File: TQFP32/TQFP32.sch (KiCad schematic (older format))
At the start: 4 parts, among them J1 Conn_01x16, J2 Conn_01x16, J3 Conn_02x16_Counter_Clockwise, J4 Conn_02x16_Counter_Clockwise

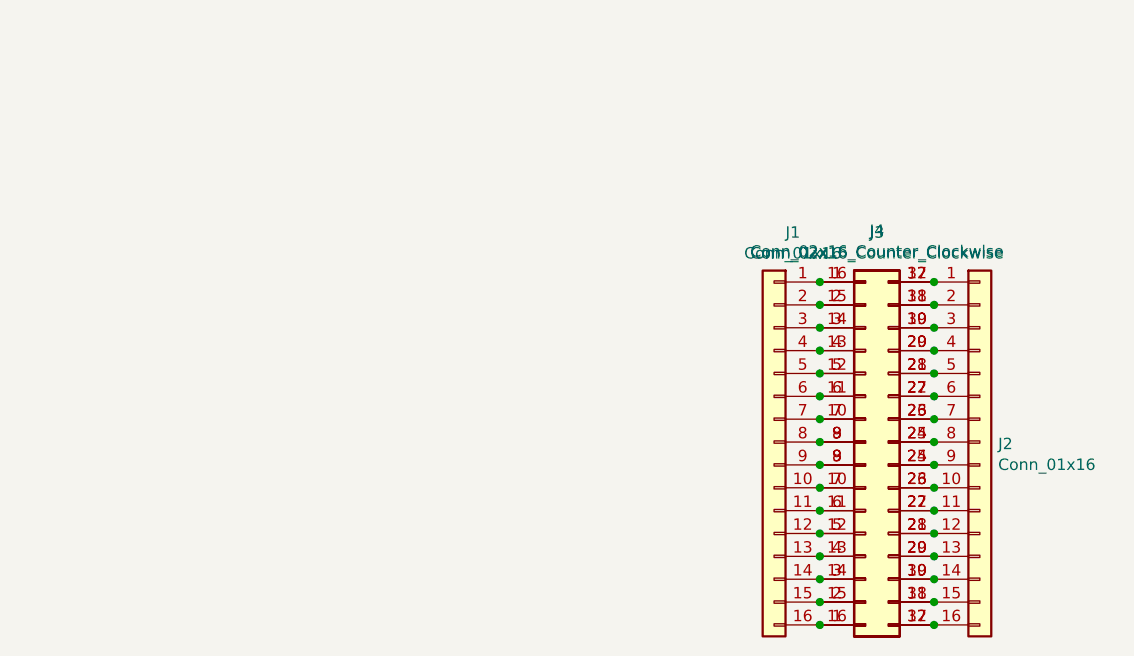
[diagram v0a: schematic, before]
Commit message: USB, SD and CR Cells Added
MicroSD, MicroUSB, MiniUSB, USB-C, CR1220, CR2032 added as well as all schematics page sizes optimised
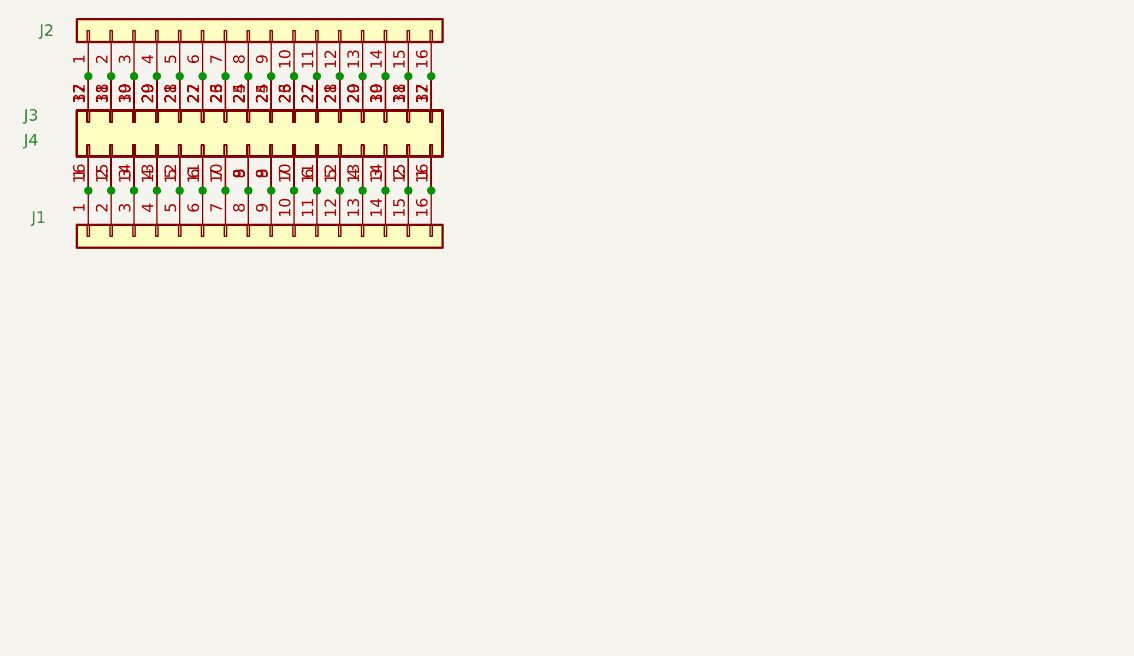
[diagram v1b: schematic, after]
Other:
- moved on the sheet: J1, J2, J3, J4
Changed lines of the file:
@@
 EESchema Schematic File Version 4
+LIBS:TQFP32-cache
 EELAYER 29 0
 EELAYER END
-$Descr A4 11693 8268
+$Descr User 5197 4016
 encoding utf-8
 Sheet 1 1
-Title ""
-Date ""
-Rev ""
-Comp ""
-Comment1 ""
-Comment2 ""
-Comment3 ""
+Title "TQFP32 to DIP32 Breakout Board"
+Date "2019-07-04"
+Rev "1"
+Comp "SirBoard"
+Comment1 "TQFP32 P = 0.8mm"
+Comment2 "LQFP32 P = 0.5mm"
+Comment3 "DIP32 P = 2.54mm"
 Comment4 ""
 $EndDescr
@@
 L Connector_Generic:Conn_01x16 J2
 U 1 1 5D1E2D5B
-P 5750 2700
-F 0 "J2" H 5830 2692 50  0000 L CNN
-F 1 "Conn_01x16" H 5830 2601 50  0000 L CNN
-F 2 "Connector_PinHeader_2.54mm:PinHeader_1x16_P2.54mm_Vertical" H 5750 2700 50  0001 C CNN
-F 3 "~" H 5750 2700 50  0001 C CNN
-	1    5750 2700
-	1    0    0    -1
+P 2550 900
+F 0 "J2" V 2550 1750 50  0000 L CNN
+F 1 "Conn_01x16" V 2630 801 50  0001 L CNN
+F 2 "Connector_PinHeader_2.54mm:PinHeader_1x16_P2.54mm_Vertical" H 2550 900 50  0001 C CNN
+F 3 "~" H 2550 900 50  0001 C CNN
+	1    2550 900
+	0    -1   -1   0
 $EndComp
 $Comp
 L Connector_Generic:Conn_02x16_Counter_Clockwise J3
 U 1 1 5D1E33BB
-P 5250 2700
-F 0 "J3" H 5300 3617 50  0000 C CNN
-F 1 "Conn_02x16_Counter_Clockwise" H 5300 3526 50  0000 C CNN
-F 2 "Package_QFP:TQFP-32_7x7mm_P0.8mm" H 5250 2700 50  0001 C CNN
-F 3 "~" H 5250 2700 50  0001 C CNN
-	1    5250 2700
-	1    0    0    -1
+P 2550 1400
+F 0 "J3" V 2650 2350 50  0000 C TNN
+F 1 "Conn_02x16_Counter_Clockwise" H 2600 2226 50  0001 C CNN
+F 2 "Package_QFP:TQFP-32_7x7mm_P0.8mm" H 2550 1400 50  0001 C CNN
+F 3 "~" H 2550 1400 50  0001 C CNN
+	1    2550 1400
+	0    -1   -1   0
 $EndComp
 $Comp
 L Connector_Generic:Conn_01x16 J1
 U 1 1 5D1E5C1F
-P 4850 2700
-F 0 "J1" H 4768 3617 50  0000 C CNN
-F 1 "Conn_01x16" H 4768 3526 50  0000 C CNN
-F 2 "Connector_PinHeader_2.54mm:PinHeader_1x16_P2.54mm_Vertical" H 4850 2700 50  0001 C CNN
-F 3 "~" H 4850 2700 50  0001 C CNN
-	1    4850 2700
-	-1   0    0    -1
+P 2550 1800
+F 0 "J1" V 2468 2717 50  0000 C CNN
+F 1 "Conn_01x16" H 2468 2626 50  0001 C CNN
+F 2 "Connector_PinHeader_2.54mm:PinHeader_1x16_P2.54mm_Vertical" H 2550 1800 50  0001 C CNN
+F 3 "~" H 2550 1800 50  0001 C CNN
+	1    2550 1800
+	0    -1   1    0
 $EndComp
 $Comp
 L Connector_Generic:Conn_02x16_Counter_Clockwise J4
 U 1 1 5D1ED9F2
-P 5250 2800
-F 0 "J4" H 5300 1775 50  0000 C CNN
-F 1 "Conn_02x16_Counter_Clockwise" H 5300 1866 50  0000 C CNN
-F 2 "Package_QFP:LQFP-32_5x5mm_P0.5mm" H 5250 2800 50  0001 C CNN
-F 3 "~" H 5250 2800 50  0001 C CNN
-	1    5250 2800
-	1    0    0    1
+P 2650 1400
+F 0 "J4" V 2700 350 50  0000 C BNN
+F 1 "Conn_02x16_Counter_Clockwise" H 2700 466 50  0001 C CNN
+F 2 "Package_QFP:LQFP-32_5x5mm_P0.5mm" H 2650 1400 50  0001 C CNN
+F 3 "~" H 2650 1400 50  0001 C CNN
+	1    2650 1400
+	0    1    -1   0
 $EndComp
-Connection ~ 5050 2000
-Connection ~ 5050 2100
-Connection ~ 5050 2200
-Connection ~ 5050 2300
-Connection ~ 5050 2400
-Connection ~ 5050 2500
-Connection ~ 5050 2600
-Connection ~ 5050 2700
-Connection ~ 5050 2800
-Connection ~ 5050 2900
-Connection ~ 5050 3000
-Connection ~ 5050 3100
-Connection ~ 5050 3200
-Connection ~ 5050 3300
-Connection ~ 5050 3400
-Connection ~ 5050 3500
-Connection ~ 5550 2000
-Connection ~ 5550 2100
-Connection ~ 5550 2200
-Connection ~ 5550 2300
-Connection ~ 5550 2400
-Connection ~ 5550 2500
-Connection ~ 5550 2600
-Connection ~ 5550 2700
-Connection ~ 5550 2800
-Connection ~ 5550 2900
-Connection ~ 5550 3000
-Connection ~ 5550 3100
-Connection ~ 5550 3200
-Connection ~ 5550 3300
-Connection ~ 5550 3400
-Connection ~ 5550 3500
+Connection ~ 1850 1600
+Connection ~ 1950 1600
+Connection ~ 2050 1600
+Connection ~ 2150 1600
+Connection ~ 2250 1600
+Connection ~ 2350 1600
+Connection ~ 2450 1600
+Connection ~ 2550 1600
+Connection ~ 2650 1600
+Connection ~ 2750 1600
+Connection ~ 2850 1600
+Connection ~ 2950 1600
+Connection ~ 3050 1600
+Connection ~ 3150 1600
+Connection ~ 3250 1600
+Connection ~ 3350 1600
+Connection ~ 1850 1100
+Connection ~ 1950 1100
+Connection ~ 2050 1100
+Connection ~ 2150 1100
+Connection ~ 2250 1100
+Connection ~ 2350 1100
+Connection ~ 2450 1100
+Connection ~ 2550 1100
+Connection ~ 2650 1100
+Connection ~ 2750 1100
+Connection ~ 2850 1100
+Connection ~ 2950 1100
+Connection ~ 3050 1100
+Connection ~ 3150 1100
+Connection ~ 3250 1100
+Connection ~ 3350 1100
 $EndSCHEMATC

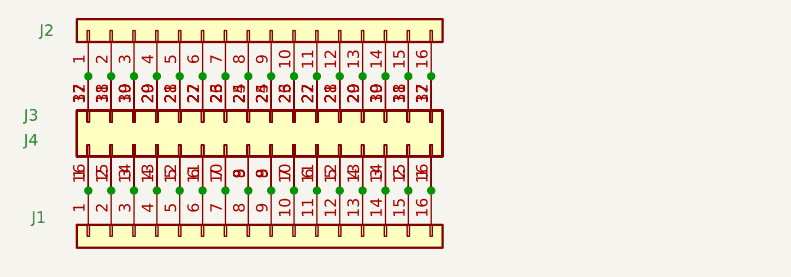
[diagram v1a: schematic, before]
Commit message: Breakout Boards Revision 2
Renders updated, silkscreen text improved, blurry silkscreen items removed/resized.
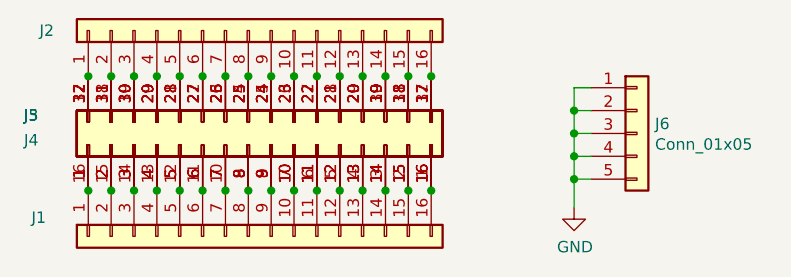
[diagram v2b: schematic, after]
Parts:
- added J5: Conn_02x16_Counter_Clockwise, Package_DFN_QFN:QFN-32-1EP_4x4mm_P0.4mm_EP2.65x2.65mm, symbol Connector_Generic:Conn_02x16_Counter_Clockwise
- added J6: Conn_01x05, Connector_PinHeader_2.54mm:PinHeader_1x05_P2.54mm_Vertical, symbol Connector_Generic:Conn_01x05
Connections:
- net at J2.1 (Pin_1), J3.32 (Pin_32), J4.17 (Pin_17): now also J5.32 (Pin_32)
- net at J2.10 (Pin_10), J3.23 (Pin_23), J4.26 (Pin_26): now also J5.23 (Pin_23)
- net at J2.11 (Pin_11), J3.22 (Pin_22), J4.27 (Pin_27): now also J5.22 (Pin_22)
- net at J2.12 (Pin_12), J3.21 (Pin_21), J4.28 (Pin_28): now also J5.21 (Pin_21)
- net at J2.13 (Pin_13), J3.20 (Pin_20), J4.29 (Pin_29): now also J5.20 (Pin_20)
- net at J2.14 (Pin_14), J3.19 (Pin_19), J4.30 (Pin_30): now also J5.19 (Pin_19)
- net at J2.15 (Pin_15), J3.18 (Pin_18), J4.31 (Pin_31): now also J5.18 (Pin_18)
- net at J2.16 (Pin_16), J3.17 (Pin_17), J4.32 (Pin_32): now also J5.17 (Pin_17)
- net at J2.2 (Pin_2), J3.31 (Pin_31), J4.18 (Pin_18): now also J5.31 (Pin_31)
- net at J2.3 (Pin_3), J3.30 (Pin_30), J4.19 (Pin_19): now also J5.30 (Pin_30)
- net at J2.4 (Pin_4), J3.29 (Pin_29), J4.20 (Pin_20): now also J5.29 (Pin_29)
- net at J2.5 (Pin_5), J3.28 (Pin_28), J4.21 (Pin_21): now also J5.28 (Pin_28)
- net at J2.6 (Pin_6), J3.27 (Pin_27), J4.22 (Pin_22): now also J5.27 (Pin_27)
- net at J2.7 (Pin_7), J3.26 (Pin_26), J4.23 (Pin_23): now also J5.26 (Pin_26)
- net at J2.8 (Pin_8), J3.25 (Pin_25), J4.24 (Pin_24): now also J5.25 (Pin_25)
- net at J2.9 (Pin_9), J3.24 (Pin_24), J4.25 (Pin_25): now also J5.24 (Pin_24)
- net at J1.1 (Pin_1), J3.1 (Pin_1), J4.16 (Pin_16): now also J5.1 (Pin_1)
- net at J1.10 (Pin_10), J3.10 (Pin_10), J4.7 (Pin_7): now also J5.10 (Pin_10)
- net at J1.11 (Pin_11), J3.11 (Pin_11), J4.6 (Pin_6): now also J5.11 (Pin_11)
- net at J1.12 (Pin_12), J3.12 (Pin_12), J4.5 (Pin_5): now also J5.12 (Pin_12)
- net at J1.13 (Pin_13), J3.13 (Pin_13), J4.4 (Pin_4): now also J5.13 (Pin_13)
- net at J1.14 (Pin_14), J3.14 (Pin_14), J4.3 (Pin_3): now also J5.14 (Pin_14)
- net at J1.15 (Pin_15), J3.15 (Pin_15), J4.2 (Pin_2): now also J5.15 (Pin_15)
- net at J1.16 (Pin_16), J3.16 (Pin_16), J4.1 (Pin_1): now also J5.16 (Pin_16)
- net at J1.2 (Pin_2), J3.2 (Pin_2), J4.15 (Pin_15): now also J5.2 (Pin_2)
- net at J1.3 (Pin_3), J3.3 (Pin_3), J4.14 (Pin_14): now also J5.3 (Pin_3)
- net at J1.4 (Pin_4), J3.4 (Pin_4), J4.13 (Pin_13): now also J5.4 (Pin_4)
- net at J1.5 (Pin_5), J3.5 (Pin_5), J4.12 (Pin_12): now also J5.5 (Pin_5)
- net at J1.6 (Pin_6), J3.6 (Pin_6), J4.11 (Pin_11): now also J5.6 (Pin_6)
- net at J1.7 (Pin_7), J3.7 (Pin_7), J4.10 (Pin_10): now also J5.7 (Pin_7)
- net at J1.8 (Pin_8), J3.8 (Pin_8), J4.9 (Pin_9): now also J5.8 (Pin_8)
- net at J1.9 (Pin_9), J3.9 (Pin_9), J4.8 (Pin_8): now also J5.9 (Pin_9)
- new net GND: J6.1 (Pin_1), J6.2 (Pin_2), J6.3 (Pin_3), J6.4 (Pin_4), J6.5 (Pin_5)
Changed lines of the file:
@@
 	0    1    -1   0
 $EndComp
+$Comp
+L Connector_Generic:Conn_02x16_Counter_Clockwise J5
+U 1 1 5E9B48D2
+P 2550 1400
+F 0 "J5" V 2650 2350 50  0000 C TNN
+F 1 "Conn_02x16_Counter_Clockwise" H 2600 2226 50  0001 C CNN
+F 2 "Package_DFN_QFN:QFN-32-1EP_4x4mm_P0.4mm_EP2.65x2.65mm" H 2550 1400 50  0001 C CNN
+F 3 "~" H 2550 1400 50  0001 C CNN
+	1    2550 1400
+	0    -1   -1   0
+$EndComp
+Connection ~ 1850 1100
 Connection ~ 1850 1600
+Connection ~ 1950 1100
 Connection ~ 1950 1600
+Connection ~ 2050 1100
 Connection ~ 2050 1600
+Connection ~ 2150 1100
 Connection ~ 2150 1600
+Connection ~ 2250 1100
 Connection ~ 2250 1600
+Connection ~ 2350 1100
 Connection ~ 2350 1600
+Connection ~ 2450 1100
 Connection ~ 2450 1600
+Connection ~ 2550 1100
 Connection ~ 2550 1600
+Connection ~ 2650 1100
 Connection ~ 2650 1600
+Connection ~ 2750 1100
 Connection ~ 2750 1600
+Connection ~ 2850 1100
 Connection ~ 2850 1600
+Connection ~ 2950 1100
 Connection ~ 2950 1600
+Connection ~ 3050 1100
 Connection ~ 3050 1600
+Connection ~ 3150 1100
 Connection ~ 3150 1600
+Connection ~ 3250 1100
 Connection ~ 3250 1600
+Connection ~ 3350 1100
 Connection ~ 3350 1600
-Connection ~ 1850 1100
-Connection ~ 1950 1100
-Connection ~ 2050 1100
-Connection ~ 2150 1100
-Connection ~ 2250 1100
-Connection ~ 2350 1100
-Connection ~ 2450 1100
-Connection ~ 2550 1100
-Connection ~ 2650 1100
-Connection ~ 2750 1100
-Connection ~ 2850 1100
-Connection ~ 2950 1100
-Connection ~ 3050 1100
-Connection ~ 3150 1100
-Connection ~ 3250 1100
-Connection ~ 3350 1100
+$Comp
+L Connector_Generic:Conn_01x05 J6
+U 1 1 5E9E639F
+P 4250 1350
+F 0 "J6" H 4329 1392 50  0000 L CNN
+F 1 "Conn_01x05" H 4329 1302 50  0000 L CNN
+F 2 "Connector_PinHeader_2.54mm:PinHeader_1x05_P2.54mm_Vertical" H 4250 1350 50  0001 C CNN
+F 3 "~" H 4250 1350 50  0001 C CNN
+	1    4250 1350
+	1    0    0    -1
+$EndComp
+$Comp
+L power:GND #PWR0101
+U 1 1 5E9E7D40
+P 3975 1675
+F 0 "#PWR0101" H 3975 1425 50  0001 C CNN
+F 1 "GND" H 3979 1503 50  0000 C CNN
+F 2 "" H 3975 1675 50  0001 C CNN
+F 3 "" H 3975 1675 50  0001 C CNN
+	1    3975 1675
+	1    0    0    -1
+$EndComp
+Wire Wire Line
+	3975 1675 3975 1550
+Wire Wire Line
+	3975 1150 4050 1150
+Wire Wire Line
+	4050 1250 3975 1250
+Connection ~ 3975 1250
+Wire Wire Line
+	3975 1250 3975 1150
+Wire Wire Line
+	3975 1350 4050 1350
+Connection ~ 3975 1350
+Wire Wire Line
+	3975 1350 3975 1250
+Wire Wire Line
+	4050 1450 3975 1450
+Connection ~ 3975 1450
+Wire Wire Line
+	3975 1450 3975 1350
+Wire Wire Line
+	3975 1550 4050 1550
+Connection ~ 3975 1550
+Wire Wire Line
+	3975 1550 3975 1450
 $EndSCHEMATC
